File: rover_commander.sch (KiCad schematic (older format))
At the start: 75 parts, among them Q1 Crystal KX-7 25MHz, Q2 Crystal KX-7 25MHz, U1 RTL8201CP, U2 L7805ABD2T-TR, U3 H1102NLT, U4 LD1117S33TR_SOT223, U5 STM32F107RCTx, U6 TJA1040T, U7 M95160-WMN6TP

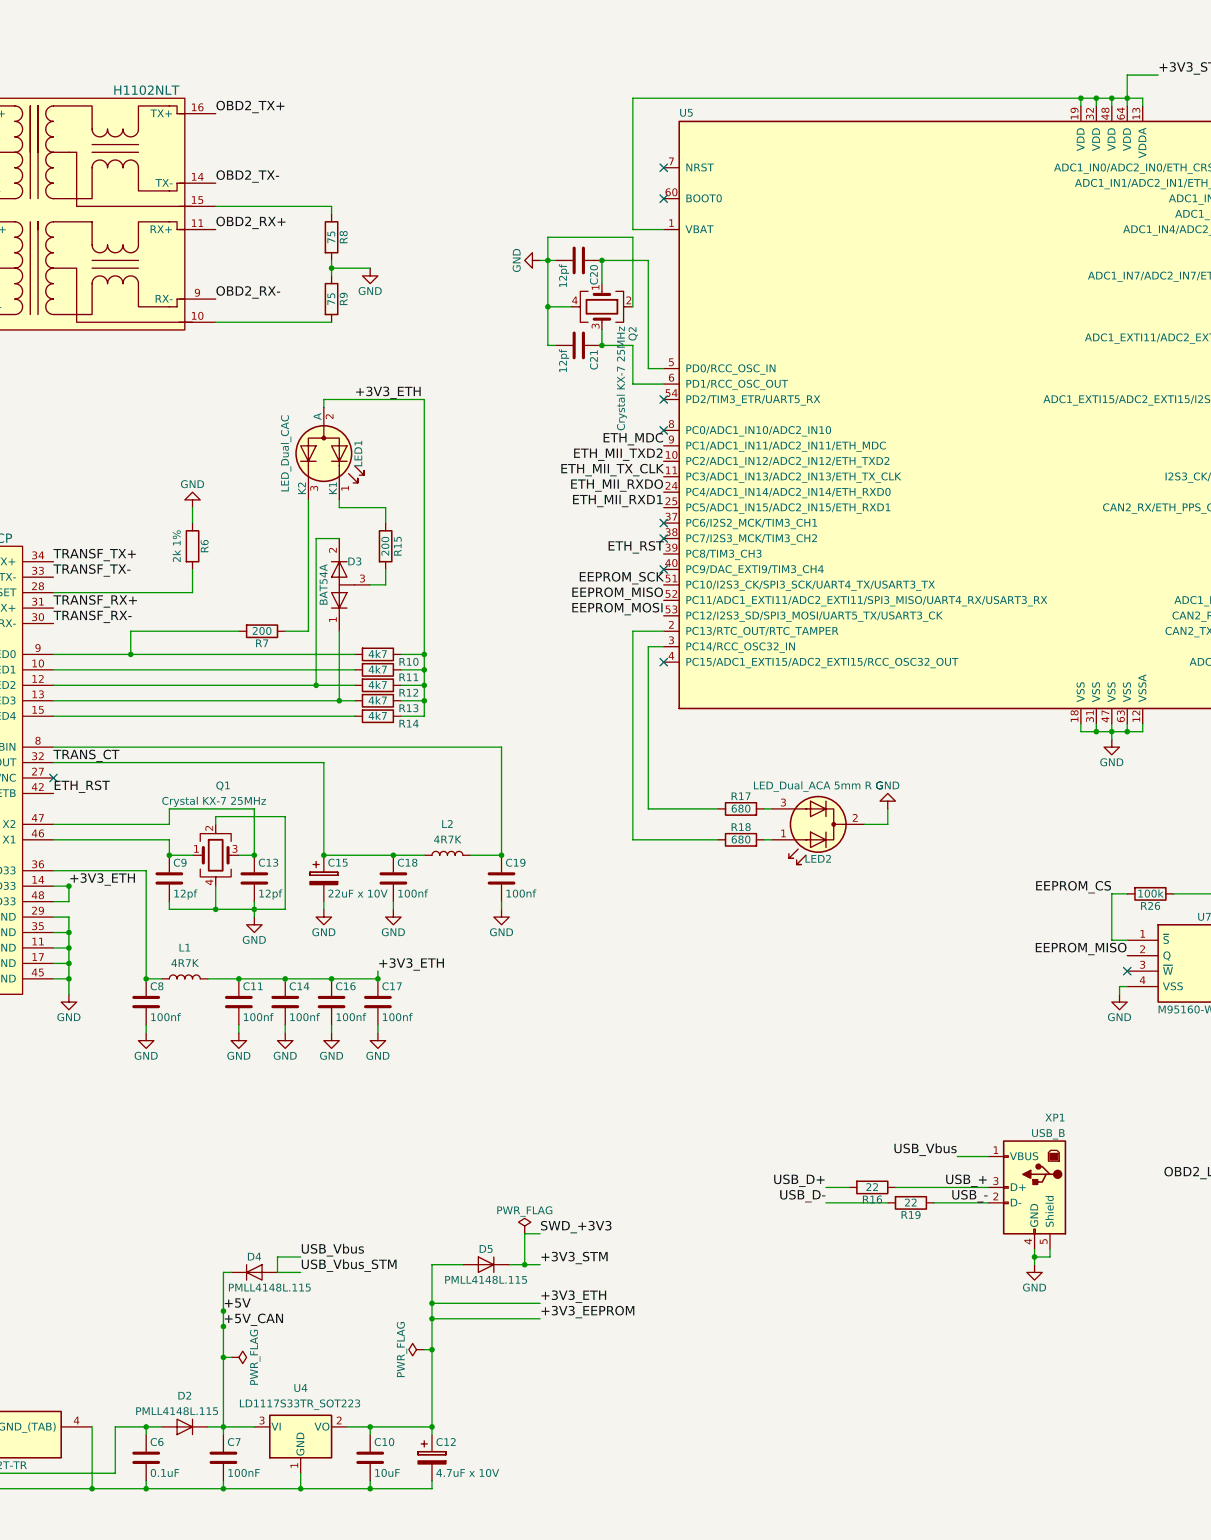
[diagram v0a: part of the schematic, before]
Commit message: power fix, diods replace with shottky, eeprom package, extra pull-up on reset
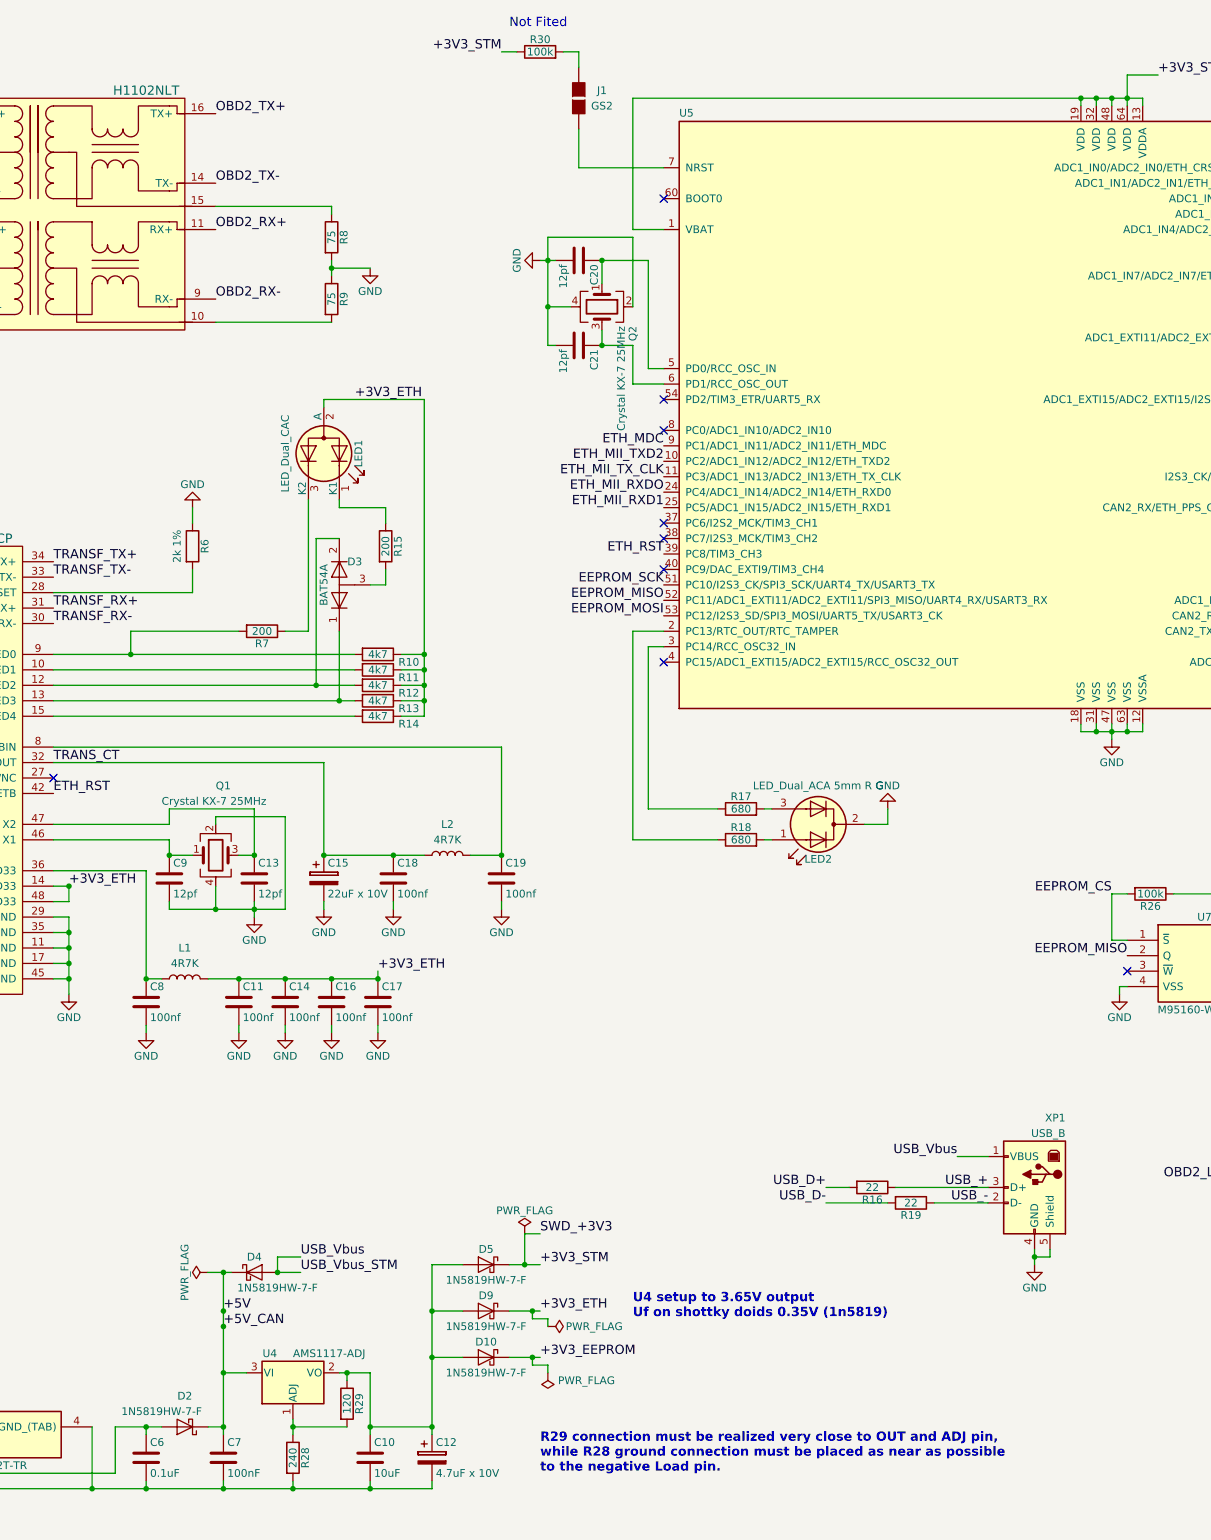
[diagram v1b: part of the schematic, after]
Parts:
- removed D2, D4: PMLL4148L.115, Diodes_SMD:D_SC-80, symbol D
- removed D5: PMLL4148L.115, Diodes_SMD:D_SC-80_HandSoldering, symbol D
- removed U4: LD1117S33TR_SOT223, TO_SOT_Packages_SMD:SOT-223-3Lead_TabPin2, symbol LD1117S33TR_SOT223
- added D10, D2, D4, D5, D9: 1N5819HW-7-F, Diodes_SMD:D_SOD-123, symbol D_Schottky
- added J1: GS2, Connectors:GS2, symbol GS2
- added R28: 240, Resistors_SMD:R_0603_HandSoldering, symbol R
- added R29: 120, Resistors_SMD:R_0603_HandSoldering, symbol R
- added R30: 100k, Resistors_SMD:R_0603_HandSoldering, symbol R
- added U4: AMS1117-ADJ, TO_SOT_Packages_SMD:SOT-223-3Lead_TabPin2, symbol LM1117-ADJ
- U7: footprint Housings_SOIC:SO-8_5.3x6.2mm_Pitch1.27mm -> Housings_SOIC:SOIC-8_3.9x4.9mm_Pitch1.27mm
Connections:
- net +3V3_EEPROM: now also D10.1 (K); no longer C10.1, C11.1, C12.1, C14.1, C16.1, C17.1, L1.2, LED1.2 (A), R10.1, R11.1, R12.1, R13.1, R14.1, R2.2, U1.14 (DVDD33), U1.37 (ANE), U1.38 (DUPLEX), U1.39 (SPEED), U1.41 (LDPS), U1.43 (ISOLATE), U1.48 (DVDD33)
- net +3V3_STM: now also D5.1 (K), R30.1
- net +5V: now also D2.1 (K), D4.1 (K), U4.3 (VI)
- net GND: now also R28.2
- net USB_Vbus: now also D4.2 (A)
- net at U5.7 (NRST): now also J1.1 (G1)
- net at C6.1, U2.3 (OUTPUT): now also D2.2 (A)
- new net: C10.1, C12.1, D10.2 (A), D5.2 (A), D9.2 (A), R29.1, U4.2 (VO)
- new net: R28.1, R29.2, U4.1 (ADJ)
- new net: J1.2 (G2), R30.2
- new net +3V3_ETH: C11.1, C14.1, C16.1, C17.1, D9.1 (K), L1.2, LED1.2 (A), R10.1, R11.1, R12.1, R13.1, R14.1, R2.2, U1.14 (DVDD33), U1.37 (ANE), U1.38 (DUPLEX), U1.39 (SPEED), U1.41 (LDPS), U1.43 (ISOLATE), U1.48 (DVDD33)
- no-connect marks 22 -> 21
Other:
- note added: "Not Fited"
- note added: "R29 connection must be realized very close to OUT and ADJ pin,\nwhile R28 ground connection must be placed as near as possible\nto the negative Load pin."
- note added: "U4 setup to 3.65V output\nUf on shottky doids 0.35V (1n5819)"

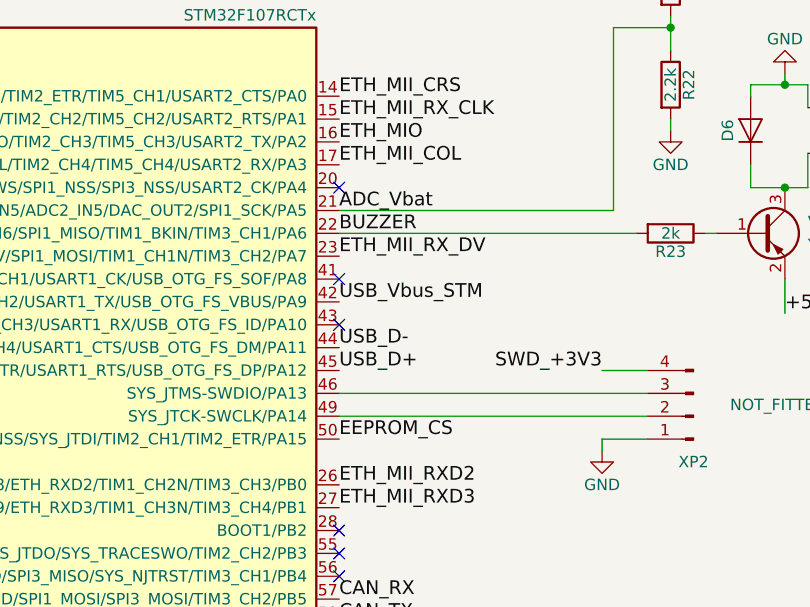
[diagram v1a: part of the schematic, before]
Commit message: fix eeprom NSS pin to correct one
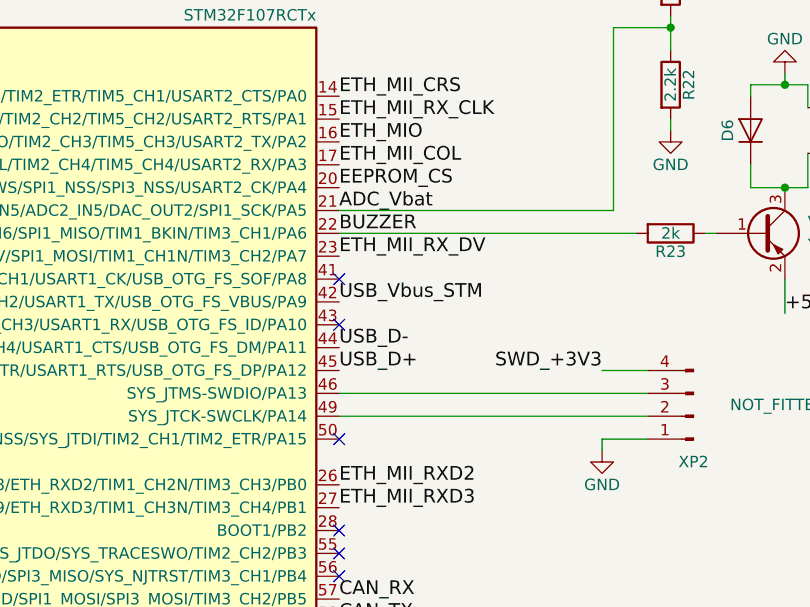
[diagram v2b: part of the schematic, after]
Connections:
- net EEPROM_CS: now also U5.20 (ADC1_IN4/ADC2_IN4/DAC_OUT1/I2S3_WS/SPI1_NSS/SPI3_NSS/USART2_CK/PA4); no longer U5.50 (ADC1_EXTI15/ADC2_EXTI15/I2S3_WS/SPI1_NSS/SPI3_NSS/SYS_JTDI/TIM2_CH1/TIM2_ETR/PA15)
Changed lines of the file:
@@
 	0    -1   -1   0
 $EndComp
-NoConn ~ 13200 2500
+NoConn ~ 13200 3600
 NoConn ~ 13200 2900
 NoConn ~ 13200 3100
@@
 Text Label 11400 7400 0    60   ~ 0
 EEPROM_MOSI
-Text Label 13200 3600 0    60   ~ 0
+Text Label 13200 2500 0    60   ~ 0
 EEPROM_CS
 Text Label 10300 6800 2    60   ~ 0

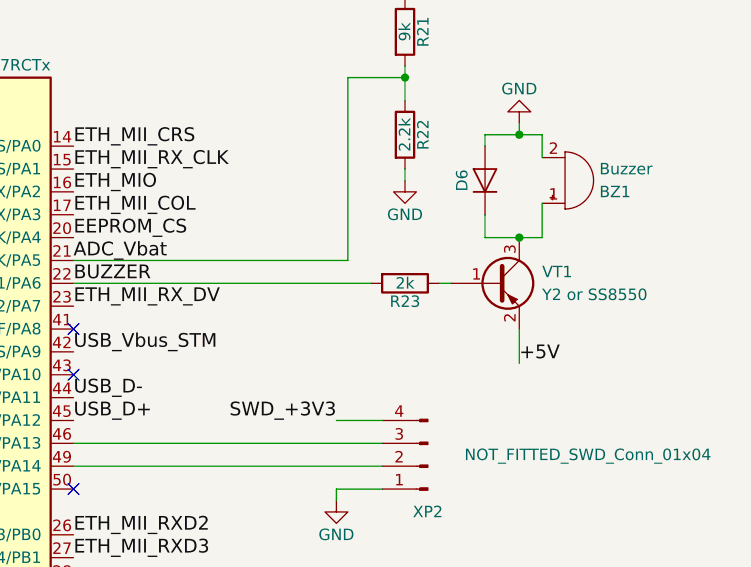
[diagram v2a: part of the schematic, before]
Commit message: fix stm32 footprint as advised in datasheet, fix libs paths
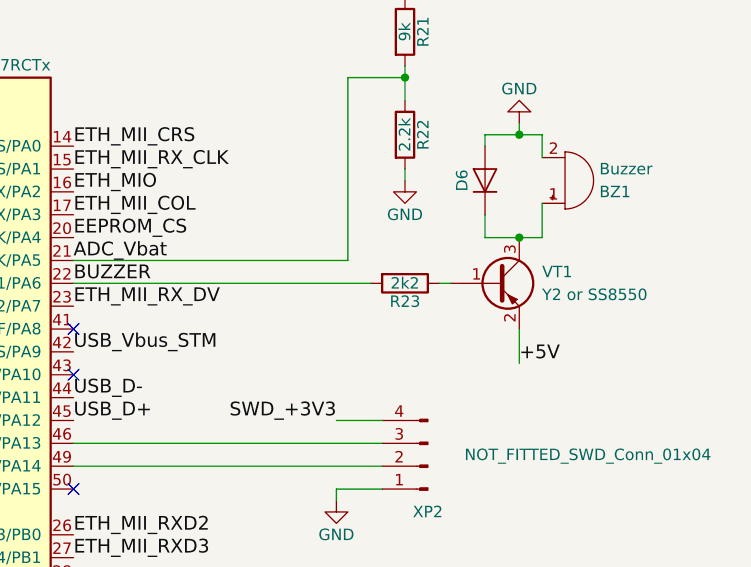
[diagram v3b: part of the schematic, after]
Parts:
- R23: value 2k -> 2k2
- U5: footprint Housings_QFP:LQFP-64_10x10mm_Pitch0.5mm -> zulljon:LQFP-64_10x10mm_Pitch0.5mm_datesheet
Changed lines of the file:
@@
 LIBS:valves
 LIBS:stm32
+LIBS:zpkl
 LIBS:M95160-WMN6TP
 LIBS:L7805ABD2T-TR
@@
 LIBS:RTL8201CP
 LIBS:h1102nlt
+LIBS:STM32F105RCT6
 LIBS:rover_commander-cache
 EELAYER 25 0
@@
 F 0 "U5" H 7500 5625 50  0000 L BNN
 F 1 "STM32F107RCTx" H 13100 5625 50  0000 R BNN
-F 2 "Housings_QFP:LQFP-64_10x10mm_Pitch0.5mm" H 13100 5575 50  0001 R TNN
+F 2 "zulljon:LQFP-64_10x10mm_Pitch0.5mm_datesheet" H 13100 5575 50  0001 R TNN
 F 3 "" H 10300 3700 50  0001 C CNN
 	1    10300 3700
@@
 P 14650 2700
 F 0 "R23" V 14730 2700 50  0000 C CNN
-F 1 "2k" V 14650 2700 50  0000 C CNN
+F 1 "2k2" V 14650 2700 50  0000 C CNN
 F 2 "Resistors_SMD:R_0603_HandSoldering" V 14580 2700 50  0001 C CNN
 F 3 "" H 14650 2700 50  0001 C CNN

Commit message: add blue LED on power supplier of stm32
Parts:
- added D11: LED BLUE, LEDs:LED_0603_HandSoldering, symbol LED
- added R31: 1k, Resistors_SMD:R_0603_HandSoldering, symbol R
- R22: value 2.2k -> 2k2
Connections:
- net labels added: +3V65
- wire segments 253 -> 257
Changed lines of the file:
@@
 P 14650 2050
 F 0 "R22" V 14730 2050 50  0000 C CNN
-F 1 "2.2k" V 14650 2050 50  0000 C CNN
+F 1 "2k2" V 14650 2050 50  0000 C CNN
 F 2 "Resistors_SMD:R_0603_HandSoldering" V 14580 2050 50  0001 C CNN
 F 3 "" H 14650 2050 50  0001 C CNN
@@
 Wire Wire Line
 	5900 9800 6100 9800
+$Comp
+L LED D11
+U 1 1 5B02D814
+P 8400 7450
+F 0 "D11" H 8400 7250 50  0000 C CNN
+F 1 "LED BLUE" H 8400 7350 50  0000 C CNN
+F 2 "LEDs:LED_0603_HandSoldering" H 8400 7450 50  0001 C CNN
+F 3 "" H 8400 7450 50  0001 C CNN
+	1    8400 7450
+	-1   0    0    1
+$EndComp
+Text Label 5550 10250 0    60   ~ 0
++3V65
+Text Label 7550 7450 0    60   ~ 0
++3V65
+$Comp
+L R R31
+U 1 1 5B02E4A1
+P 8000 7450
+F 0 "R31" V 8080 7450 50  0000 C CNN
+F 1 "1k" V 8000 7450 50  0000 C CNN
+F 2 "Resistors_SMD:R_0603_HandSoldering" V 7930 7450 50  0001 C CNN
+F 3 "" H 8000 7450 50  0001 C CNN
+	1    8000 7450
+	0    -1   -1   0
+$EndComp
+Wire Wire Line
+	8150 7450 8250 7450
+Wire Wire Line
+	8550 7450 8600 7450
+Wire Wire Line
+	8600 7450 8600 7500
+Wire Wire Line
+	7550 7450 7850 7450
+$Comp
+L GND #PWR038
+U 1 1 5B02F849
+P 8600 7500
+F 0 "#PWR038" H 8600 7250 50  0001 C CNN
+F 1 "GND" H 8600 7350 50  0000 C CNN
+F 2 "" H 8600 7500 50  0001 C CNN
+F 3 "" H 8600 7500 50  0001 C CNN
+	1    8600 7500
+	1    0    0    -1
+$EndComp
 $EndSCHEMATC
